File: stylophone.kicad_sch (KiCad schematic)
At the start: 69 parts, among them J2 USB_C, SW1 PWR, U1 NA555P

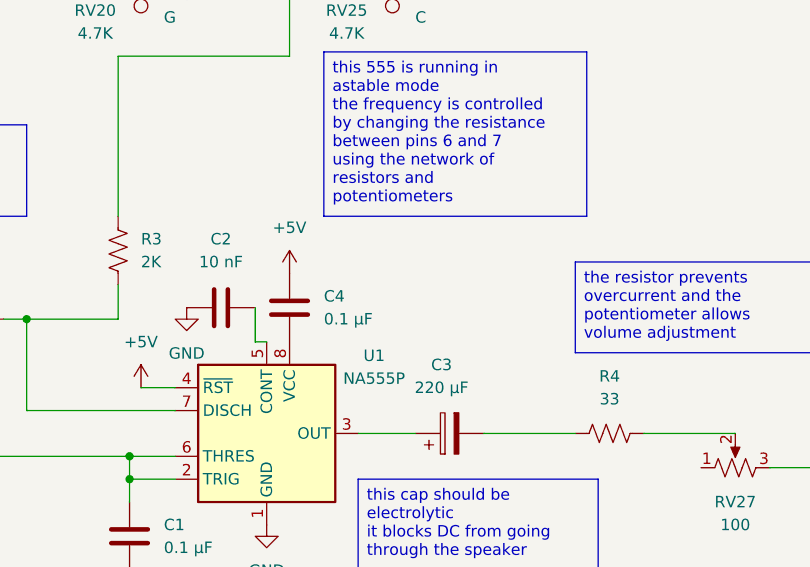
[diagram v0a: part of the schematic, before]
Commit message: fix decoupling capacitor
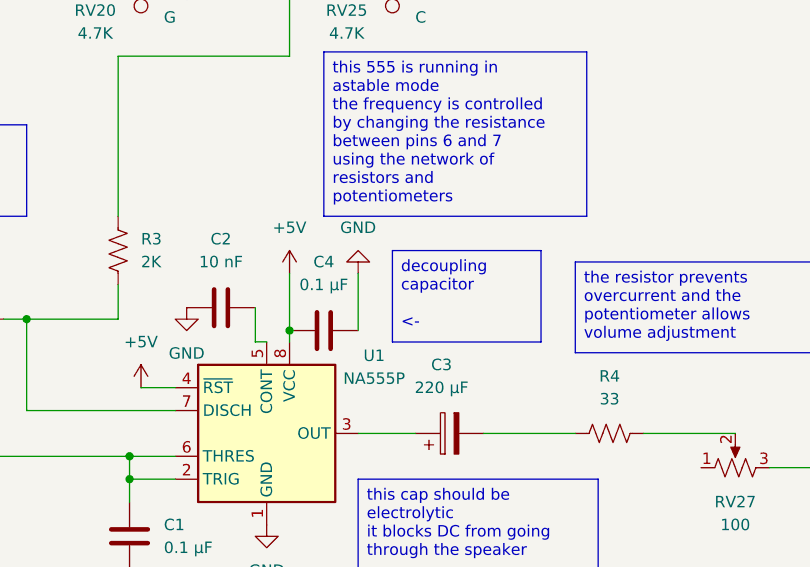
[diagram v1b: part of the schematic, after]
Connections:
- net +5V: now also U1.8 (VCC)
- net GND: now also C4.1
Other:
- moved on the sheet: C4
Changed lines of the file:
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@@
 		)
 	)
+	(text_box "decoupling capacitor\n\n<-"
+		(exclude_from_sim no)
+		(at 201.93 120.65 0)
+		(size 16.51 10.16)
+		(margins 0.9525 0.9525 0.9525 0.9525)
+		(stroke
+			(width 0)
+			(type solid)
+		)
+		(fill
+			(type none)
+		)
+		(effects
+			(font
+				(size 1.27 1.27)
+			)
+			(justify left top)
+		)
+	)
 	(junction
 		(at 201.93 90.17)
@@
 	)
 	(junction
+		(at 190.5 129.54)
+		(diameter 0)
+		(color 0 0 0 0)
+	)
+	(junction
 		(at 173.99 90.17)
 		(diameter 0)
@@
 	(wire
 		(pts
+			(xy 198.12 123.19) (xy 198.12 129.54)
+		)
+		(stroke
+			(width 0)
+			(type default)
+		)
+	)
+	(wire
+		(pts
 			(xy 85.09 86.36) (xy 104.14 86.36)
 		)
@@
 	(wire
 		(pts
+			(xy 190.5 123.19) (xy 190.5 130.81)
+		)
+		(stroke
+			(width 0)
+			(type default)
+		)
+	)
+	(wire
+		(pts
 			(xy 168.91 86.36) (xy 187.96 86.36)
 		)
@@
 	(symbol
 		(lib_id "Device:C")
-		(at 190.5 127 180)
+		(at 194.31 129.54 270)
 		(unit 1)
 		(body_style 1)
@@
 		(fields_autoplaced yes)
 		(property "Reference" "C4"
-			(at 194.31 125.7299 0)
+			(at 194.31 121.92 90)
 			(show_name no)
 			(do_not_autoplace no)
@@
 					(size 1.27 1.27)
 				)
-				(justify right)
 			)
 		)
 		(property "Value" "0.1 μF"
-			(at 194.31 128.2699 0)
+			(at 194.31 124.46 90)
 			(show_name no)
 			(do_not_autoplace no)
@@
 					(size 1.27 1.27)
 				)
-				(justify right)
 			)
 		)
 		(property "Footprint" "Capacitor_THT:C_Rect_L10.0mm_W3.0mm_P7.50mm_FKS3_FKP3"
-			(at 189.5348 123.19 0)
+			(at 190.5 130.5052 0)
 			(hide yes)
 			(show_name no)
@@
 		)
 		(property "Datasheet" ""
-			(at 190.5 127 0)
+			(at 194.31 129.54 0)
 			(hide yes)
 			(show_name no)
@@
 		)
 		(property "Description" "Unpolarized capacitor"
-			(at 190.5 127 0)
+			(at 194.31 129.54 0)
 			(hide yes)
 			(show_name no)
@@
 					(unit 1)
 				)
+			)
+		)
+	)
+	(symbol
+		(lib_id "power:GND")
+		(at 198.12 123.19 180)
+		(unit 1)
+		(body_style 1)
+		(exclude_from_sim no)
+		(in_bom yes)
+		(on_board yes)
+		(in_pos_files yes)
+		(dnp no)
+		(fields_autoplaced yes)
+		(property "Reference" "#PWR011"
+			(at 198.12 116.84 0)
+			(hide yes)
+			(show_name no)
+			(do_not_autoplace no)
+			(effects
+				(font
+					(size 1.27 1.27)
+				)
+			)
+		)
+		(property "Value" "GND"
+			(at 198.12 118.11 0)
+			(show_name no)
+			(do_not_autoplace no)
+			(effects
+				(font
+					(size 1.27 1.27)
+				)
+			)
+		)
+		(property "Footprint" ""
+			(at 198.12 123.19 0)
+			(hide yes)
+			(show_name no)
+			(do_not_autoplace no)
+			(effects
+				(font
+					(size 1.27 1.27)
+				)
+			)
+		)
+		(property "Datasheet" ""
+			(at 198.12 123.19 0)
+			(hide yes)
+			(show_name no)
+			(do_not_autoplace no)
+			(effects
+				(font
+					(size 1.27 1.27)
+				)
+			)
+		)
+		(property "Description" "Power symbol creates a global label with name \"GND\" , ground"
+			(at 198.12 123.19 0)
+			(hide yes)
+			(show_name no)
+			(do_not_autoplace no)
+			(effects
+				(font
+					(size 1.27 1.27)
+				)
+			)
+		)
+		(pin "1"
+		)
+		(instances
+			(project "stylophone"
+				(path "/585a5c70-ee35-4e08-a3c1-f9b174e000cc"
+					(reference "#PWR011")
+					(unit 1)
+				)

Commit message: add octaves to test pads
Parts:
- TP10: value F# -> F#_4
- TP11: value F -> F_4
- TP12: value E -> E_4
- TP13: value D# -> D#_4
- TP14: value D -> D_4
- TP15: value C# -> C#_4
- TP16: value C -> C_4
- TP17: value B -> B_3
- TP18: value A# -> A#_3
- TP19: value A -> A_3
- TP20: value G# -> G#_3
- TP21: value G -> G_3
- TP22: value F# -> F#_3
- TP23: value F -> F_3
- TP24: value E -> E_3
- TP25: value D# -> D#_3
- TP26: value D -> D_3
- TP27: value C# -> C#_3
- TP28: value C -> C_3
- TP4: value C -> C_5
- TP5: value B -> B_4
- TP6: value A# -> A#_4
- TP7: value A -> A_4
- TP8: value G# -> G#_4
- TP9: value G -> G_4
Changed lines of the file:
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@@
 			)
 		)
-		(property "Value" "C"
+		(property "Value" "C_3"
 			(at 92.71 42.6719 0)
 			(show_name no)
@@
 			)
 		)
-		(property "Value" "A"
+		(property "Value" "A_4"
 			(at 204.47 56.6419 0)
 			(show_name no)
@@
 			)
 		)
-		(property "Value" "D"
+		(property "Value" "D_3"
 			(at 92.71 69.3419 0)
 			(show_name no)
@@
 			)
 		)
-		(property "Value" "D#"
+		(property "Value" "D#_4"
 			(at 176.53 42.6719 0)
 			(show_name no)
@@
 			)
 		)
-		(property "Value" "D"
+		(property "Value" "D_4"
 			(at 148.59 94.7419 0)
 			(show_name no)
@@
 			)
 		)
-		(property "Value" "F"
+		(property "Value" "F_4"
 			(at 176.53 69.3419 0)
 			(show_name no)
@@
 			)
 		)
-		(property "Value" "F#"
+		(property "Value" "F#_4"
 			(at 176.53 82.0419 0)
 			(show_name no)
@@
 			)
 		)
-		(property "Value" "E"
+		(property "Value" "E_3"
 			(at 92.71 94.7419 0)
 			(show_name no)
@@
 			)
 		)
-		(property "Value" "G"
+		(property "Value" "G_3"
 			(at 120.65 69.3419 0)
 			(show_name no)
@@
 			)
 		)
-		(property "Value" "B"
+		(property "Value" "B_3"
 			(at 148.59 56.6419 0)
 			(show_name no)
@@
 			)
 		)
-		(property "Value" "A"
+		(property "Value" "A_3"
 			(at 120.65 94.7419 0)
 			(show_name no)
@@
 			)
 		)
-		(property "Value" "D#"
+		(property "Value" "D#_3"
 			(at 92.71 82.0419 0)
 			(show_name no)
@@
 			)
 		)
-		(property "Value" "E"
+		(property "Value" "E_4"
 			(at 176.53 56.6419 0)
 			(show_name no)
@@
 			)
 		)
-		(property "Value" "B"
+		(property "Value" "B_4"
 			(at 204.47 82.0419 0)
 			(show_name no)
@@
 			)
 		)
-		(property "Value" "G"
+		(property "Value" "G_4"
 			(at 176.53 94.7419 0)
 			(show_name no)
@@
 			)
 		)
-		(property "Value" "A#"
+		(property "Value" "A#_4"
 			(at 204.47 69.3419 0)
 			(show_name no)
@@
 			)
 		)
-		(property "Value" "C"
+		(property "Value" "C_5"
 			(at 204.47 94.7419 0)
 			(show_name no)
@@
 			)
 		)
-		(property "Value" "F"
+		(property "Value" "F_3"
 			(at 120.65 42.6719 0)
 			(show_name no)
@@
 			)
 		)
-		(property "Value" "C"
+		(property "Value" "C_4"
 			(at 148.59 69.3419 0)
 			(show_name no)
@@
 			)
 		)
-		(property "Value" "F#"
+		(property "Value" "F#_3"
 			(at 120.65 56.6419 0)
 			(show_name no)
@@
 			)
 		)
-		(property "Value" "G#"
+		(property "Value" "G#_3"
 			(at 120.65 82.0419 0)
 			(show_name no)
@@
 			)
 		)
-		(property "Value" "C#"
+		(property "Value" "C#_4"
 			(at 148.59 82.0419 0)
 			(show_name no)
@@
 			)
 		)
-		(property "Value" "A#"
+		(property "Value" "A#_3"
 			(at 148.59 42.6719 0)
 			(show_name no)
@@
 			)
 		)
-		(property "Value" "C#"
+		(property "Value" "C#_3"
 			(at 92.71 56.6419 0)
 			(show_name no)
@@
 			)
 		)
-		(property "Value" "G#"
+		(property "Value" "G#_4"
 			(at 204.47 42.6719 0)
 			(show_name no)
